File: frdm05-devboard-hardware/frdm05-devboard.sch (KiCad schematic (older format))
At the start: 63 parts, among them CON1 MIKROBUS_HOST_CONN, J1 SD_Card_Fix, J2 KEYBOARD, J3 Conn_01x06, J4 LIGHT SENSOR, J5 1602 LCD VIA I2C, Q1 BCV62, Q2 BC817, SW1 PTS810, SW2 PTS810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

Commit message: Initial commit of Rev.2 hardware
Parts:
- added C10, C11, C8, C9: 100n, Capacitor_SMD:C_0805_2012Metric_Pad1.18x1.45mm_HandSolder, symbol Device:C
- added C7: 1u, Capacitor_SMD:C_0805_2012Metric_Pad1.18x1.45mm_HandSolder, symbol Device:C
- added F1, F2: Polyfuse, Fuse:Fuse_0805_2012Metric, symbol Device:Polyfuse
- added R19: 470, Resistor_SMD:R_0805_2012Metric_Pad1.20x1.40mm_HandSolder, symbol Device:R
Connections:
- net +3V3: now also C10.2, C11.2, C7.2, C8.1, C9.2, F1.2; no longer A1.4 (3V3)
- net +5V: now also U6.5 (VCC), F2.1, R19.1; no longer A1.5 (+5V), BZ1.1 (-)
- net AN_KEYPAD: now also Q1.2 (C1); no longer Q1.1 (C2)
- net GND: now also U6.3 (GND), C10.1, C11.1, C7.1, C8.2, C9.1
- net at R4.1: now also Q1.1 (C2); no longer Q1.2 (C1)
- new net: BZ1.1 (-), R19.2
- new net: A1.4 (3V3), F1.1
- new net: A1.5 (+5V), F2.2
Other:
- note added: "Fuse ratings\nto be tested\nif not desired, 0R\nresistor can be used"
- moved on the sheet: A1, BT1, BZ1, C1, C2, C3, C4, C5, C6, CON1, D1, D2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

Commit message: Initial commit of Rev.2.1 hardware
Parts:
- BZ1: footprint Buzzer_Beeper:Buzzer_12x9.5RM7.6 -> Buzzer_Beeper:MagneticBuzzer_ProSignal_ABT-410-RC
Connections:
- net +3V3: no longer A1.2 (IOREF)
- net 3V3_UNPROT: now reaches A1.4 (3V3), F1.1
- net 3V3_UNPROT: now also A1.2 (IOREF)
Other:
- moved on the sheet: F1, F2
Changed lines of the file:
@@
 Sheet 1 1
 Title "KL05Z-EVALBOARD"
-Date "2022-01-16"
-Rev "2"
+Date "2022-01-20"
+Rev "2.1"
 Comp "AGH"
 Comment1 ""
@@
 F 0 "BZ1" H 8602 2979 50  0000 L CNN
 F 1 "Buzzer" H 8602 2888 50  0000 L CNN
-F 2 "Buzzer_Beeper:Buzzer_12x9.5RM7.6" V 8425 3050 50  0001 C CNN
+F 2 "Buzzer_Beeper:MagneticBuzzer_ProSignal_ABT-410-RC" V 8425 3050 50  0001 C CNN
 F 3 "~" V 8425 3050 50  0001 C CNN
 	1    8450 2950
@@
 L power:+3V3 #PWR0101
 U 1 1 61B33C20
-P 5550 2200
-F 0 "#PWR0101" H 5550 2050 50  0001 C CNN
-F 1 "+3V3" H 5400 2200 50  0000 C CNN
-F 2 "" H 5550 2200 50  0001 C CNN
-F 3 "" H 5550 2200 50  0001 C CNN
-	1    5550 2200
+P 5550 2150
+F 0 "#PWR0101" H 5550 2000 50  0001 C CNN
+F 1 "+3V3" H 5400 2150 50  0000 C CNN
+F 2 "" H 5550 2150 50  0001 C CNN
+F 3 "" H 5550 2150 50  0001 C CNN
+	1    5550 2150
 	1    0    0    -1
 $EndComp
@@
 L power:+5V #PWR0102
 U 1 1 61B340B7
-P 5850 2200
-F 0 "#PWR0102" H 5850 2050 50  0001 C CNN
-F 1 "+5V" H 5950 2200 50  0000 C CNN
-F 2 "" H 5850 2200 50  0001 C CNN
-F 3 "" H 5850 2200 50  0001 C CNN
-	1    5850 2200
+P 5850 2150
+F 0 "#PWR0102" H 5850 2000 50  0001 C CNN
+F 1 "+5V" H 5950 2150 50  0000 C CNN
+F 2 "" H 5850 2150 50  0001 C CNN
+F 3 "" H 5850 2150 50  0001 C CNN
+	1    5850 2150
 	1    0    0    -1
 $EndComp
@@
 	4250 1250 4300 1250
 $Comp
-L power:+3V3 #PWR0107
-U 1 1 61B69EE9
-P 6050 3250
-F 0 "#PWR0107" H 6050 3100 50  0001 C CNN
-F 1 "+3V3" V 6050 3450 50  0000 C CNN
-F 2 "" H 6050 3250 50  0001 C CNN
-F 3 "" H 6050 3250 50  0001 C CNN
-	1    6050 3250
-	0    1    1    0
-$EndComp
-$Comp
 L Graphic:SYM_ESD_Large SYM1
 U 1 1 61C72011
@@
 L Device:Polyfuse F1
 U 1 1 6238704C
-P 5550 2400
-F 0 "F1" H 5463 2354 50  0000 R CNN
-F 1 "Polyfuse" H 5463 2445 50  0000 R CNN
-F 2 "Fuse:Fuse_0805_2012Metric" H 5600 2200 50  0001 L CNN
-F 3 "~" H 5550 2400 50  0001 C CNN
-	1    5550 2400
+P 5550 2350
+F 0 "F1" H 5463 2304 50  0000 R CNN
+F 1 "Polyfuse" H 5463 2395 50  0000 R CNN
+F 2 "Fuse:Fuse_0805_2012Metric" H 5600 2150 50  0001 L CNN
+F 3 "~" H 5550 2350 50  0001 C CNN
+	1    5550 2350
 	1    0    0    1
 $EndComp
-$Comp
-L Device:Polyfuse F2
-U 1 1 62387875
-P 5850 2400
-F 0 "F2" H 5938 2446 50  0000 L CNN
-F 1 "Polyfuse" H 5938 2355 50  0000 L CNN
-F 2 "Fuse:Fuse_0805_2012Metric" H 5900 2200 50  0001 L CNN
-F 3 "~" H 5850 2400 50  0001 C CNN
-	1    5850 2400
-	1    0    0    -1
-$EndComp
-Wire Wire Line
-	5550 2550 5650 2550
 Wire Wire Line
 	5650 2550 5650 2650
 Wire Wire Line
-	5750 2650 5750 2550
-Wire Wire Line
-	5750 2550 5850 2550
-Wire Wire Line
-	5850 2250 5850 2200
-Wire Wire Line
-	5550 2250 5550 2200
+	5850 2200 5850 2150
+Wire Wire Line
+	5550 2200 5550 2150
 Text Notes 4300 2500 0    50   ~ 0
 Fuse ratings\nto be tested\nif not desired, 0R\nresistor can be used
@@
 L power:PWR_FLAG #FLG0101
 U 1 1 6248CEC8
-P 6100 2200
-F 0 "#FLG0101" H 6100 2275 50  0001 C CNN
-F 1 "PWR_FLAG" H 6100 2373 50  0000 C CNN
-F 2 "" H 6100 2200 50  0001 C CNN
-F 3 "~" H 6100 2200 50  0001 C CNN
-	1    6100 2200
+P 6100 2150
+F 0 "#FLG0101" H 6100 2225 50  0001 C CNN
+F 1 "PWR_FLAG" H 6100 2323 50  0000 C CNN
+F 2 "" H 6100 2150 50  0001 C CNN
+F 3 "~" H 6100 2150 50  0001 C CNN
+	1    6100 2150
 	1    0    0    -1
 $EndComp
@@
 L power:PWR_FLAG #FLG0103
 U 1 1 6248D33F
-P 5250 2200
-F 0 "#FLG0103" H 5250 2275 50  0001 C CNN
-F 1 "PWR_FLAG" H 5250 2373 50  0000 C CNN
-F 2 "" H 5250 2200 50  0001 C CNN
-F 3 "~" H 5250 2200 50  0001 C CNN
-	1    5250 2200
-	1    0    0    -1
-$EndComp
-Connection ~ 5550 2250
-Wire Wire Line
-	5250 2250 5250 2200
-Wire Wire Line
-	5250 2250 5550 2250
-Wire Wire Line
-	5850 2250 6100 2250
-Wire Wire Line
-	6100 2250 6100 2200
-Connection ~ 5850 2250
+P 5250 2150
+F 0 "#FLG0103" H 5250 2225 50  0001 C CNN
+F 1 "PWR_FLAG" H 5250 2323 50  0000 C CNN
+F 2 "" H 5250 2150 50  0001 C CNN
+F 3 "~" H 5250 2150 50  0001 C CNN
+	1    5250 2150
+	1    0    0    -1
+$EndComp
+Connection ~ 5550 2200
+Wire Wire Line
+	5250 2200 5250 2150
+Wire Wire Line
+	5250 2200 5550 2200
+Wire Wire Line
+	5850 2200 6100 2200
+Wire Wire Line
+	6100 2200 6100 2150
+Connection ~ 5850 2200
+$Comp
+L Device:Polyfuse F2
+U 1 1 62387875
+P 5850 2350
+F 0 "F2" H 5938 2396 50  0000 L CNN
+F 1 "Polyfuse" H 5938 2305 50  0000 L CNN
+F 2 "Fuse:Fuse_0805_2012Metric" H 5900 2150 50  0001 L CNN
+F 3 "~" H 5850 2350 50  0001 C CNN
+	1    5850 2350
+	1    0    0    -1
+$EndComp
+Wire Wire Line
+	5750 2550 5850 2550
+Wire Wire Line
+	5850 2550 5850 2500
+Wire Wire Line
+	5750 2550 5750 2650
+Wire Wire Line
+	5650 2550 5550 2550
+Wire Wire Line
+	5550 2550 5550 2500
+Text GLabel 5500 2550 0    50   Input ~ 0
+3V3_UNPROT
+Wire Wire Line
+	5500 2550 5550 2550
+Connection ~ 5550 2550
+Text GLabel 6050 3250 2    50   Input ~ 0
+3V3_UNPROT
 $EndSCHEMATC

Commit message: Initial commit of Rev.2.2 hardware
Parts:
- U6: value 74HCT1G125GV -> 74AHCT1G125GV
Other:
- note added: "74HCT1G125GV\nis too slow \nsimilar buffers from\nother manufacturers\ncan also be used"
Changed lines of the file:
@@
 Title "KL05Z-EVALBOARD"
 Date "2022-01-20"
-Rev "2.1"
+Rev "2.2"
 Comp "AGH"
 Comment1 ""
@@
 P 4600 1250
 F 0 "U6" H 4300 1400 50  0000 L CNN
-F 1 "74HCT1G125GV" H 3850 1100 50  0000 L CNN
+F 1 "74AHCT1G125GV" H 3800 1100 50  0000 L CNN
 F 2 "Package_TO_SOT_SMD:SOT-23-5_HandSoldering" H 4600 1250 50  0001 C CNN
 F 3 "" H 4600 1250 50  0001 C CNN
@@
 Wire Wire Line
 	5550 2200 5550 2150
-Text Notes 4300 2500 0    50   ~ 0
+Text Notes 4300 2400 0    50   ~ 0
 Fuse ratings\nto be tested\nif not desired, 0R\nresistor can be used
 Wire Wire Line
@@
 Text GLabel 6050 3250 2    50   Input ~ 0
 3V3_UNPROT
+Text Notes 3550 1900 0    50   ~ 0
+74HCT1G125GV\nis too slow \nsimilar buffers from\nother manufacturers\ncan also be used
 $EndSCHEMATC

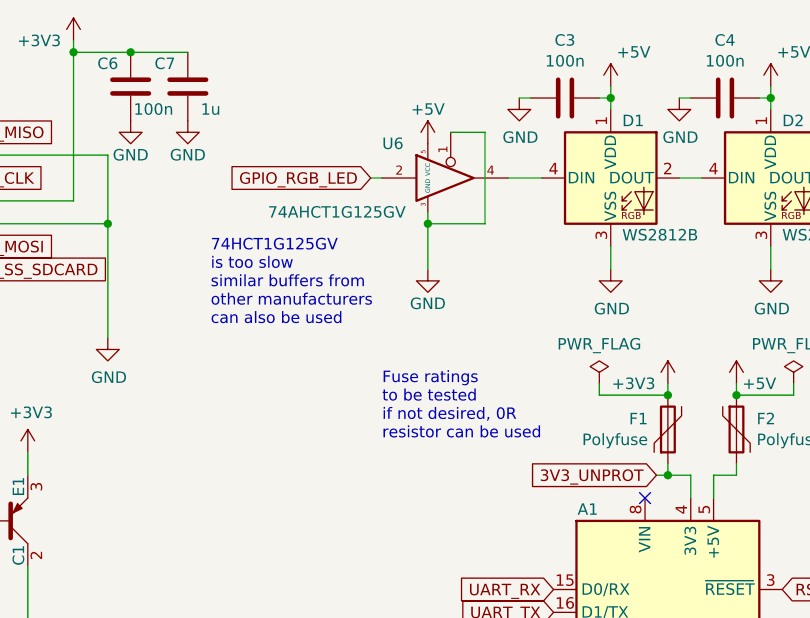
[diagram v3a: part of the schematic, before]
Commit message: Fix note about using alternative buffer for WS2812B LEDs
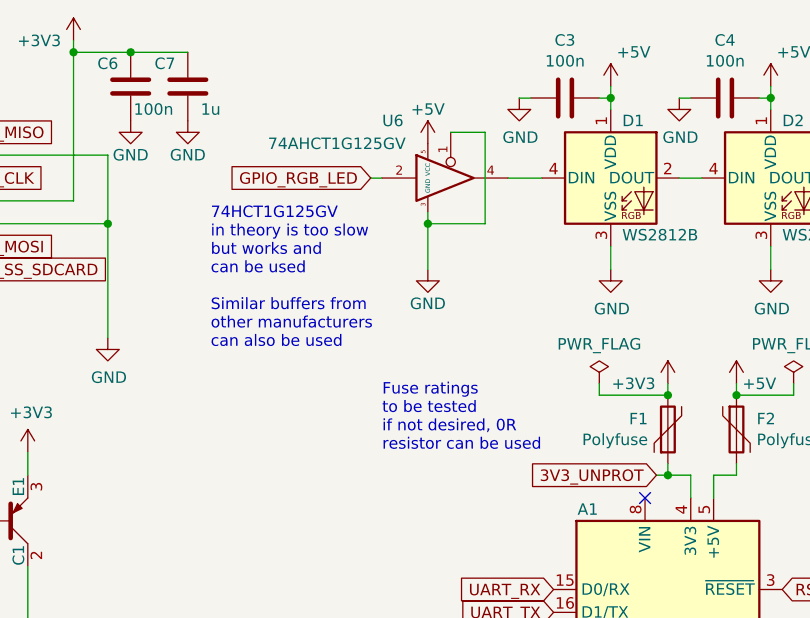
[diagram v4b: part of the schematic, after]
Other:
- note added: "74HCT1G125GV\nin theory is too slow\nbut works and \ncan be used\n\nSimilar buffers from\nother manufacturers\ncan also be used"
- note removed: "74HCT1G125GV\nis too slow \nsimilar buffers from\nother manufacturers\ncan also be used"
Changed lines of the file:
@@
 U 1 1 61CC6C67
 P 4600 1250
-F 0 "U6" H 4300 1400 50  0000 L CNN
-F 1 "74AHCT1G125GV" H 3800 1100 50  0000 L CNN
+F 0 "U6" H 4300 1500 50  0000 L CNN
+F 1 "74AHCT1G125GV" H 3800 1400 50  0000 L CNN
 F 2 "Package_TO_SOT_SMD:SOT-23-5_HandSoldering" H 4600 1250 50  0001 C CNN
 F 3 "" H 4600 1250 50  0001 C CNN
@@
 Wire Wire Line
 	5550 2200 5550 2150
-Text Notes 4300 2400 0    50   ~ 0
+Text Notes 4300 2450 0    50   ~ 0
 Fuse ratings\nto be tested\nif not desired, 0R\nresistor can be used
 Wire Wire Line
@@
 Text GLabel 6050 3250 2    50   Input ~ 0
 3V3_UNPROT
-Text Notes 3550 1900 0    50   ~ 0
-74HCT1G125GV\nis too slow \nsimilar buffers from\nother manufacturers\ncan also be used
+Text Notes 3550 2000 0    50   ~ 0
+74HCT1G125GV\nin theory is too slow\nbut works and \ncan be used\n\nSimilar buffers from\nother manufacturers\ncan also be used
 $EndSCHEMATC
